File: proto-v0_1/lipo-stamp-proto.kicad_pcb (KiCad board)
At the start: 4 copper layers, 45.7 x 45.7 mm, 109 parts, among them Q1 Q_PMOS_GSD, U3 MCP73832-2-OT, U4 AP2112K-3.3, U5 AP9101CK6, U6 FS8205

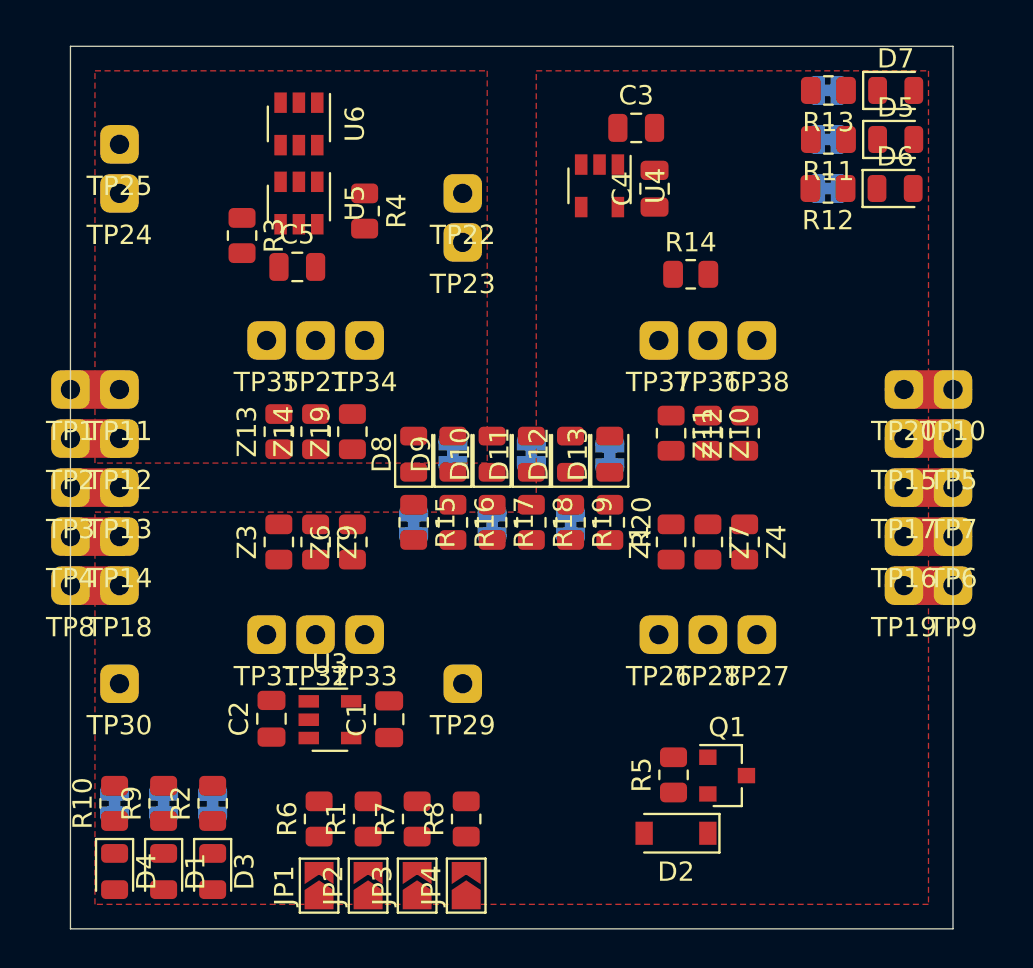
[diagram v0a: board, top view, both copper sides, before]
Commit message: Passes DRC now
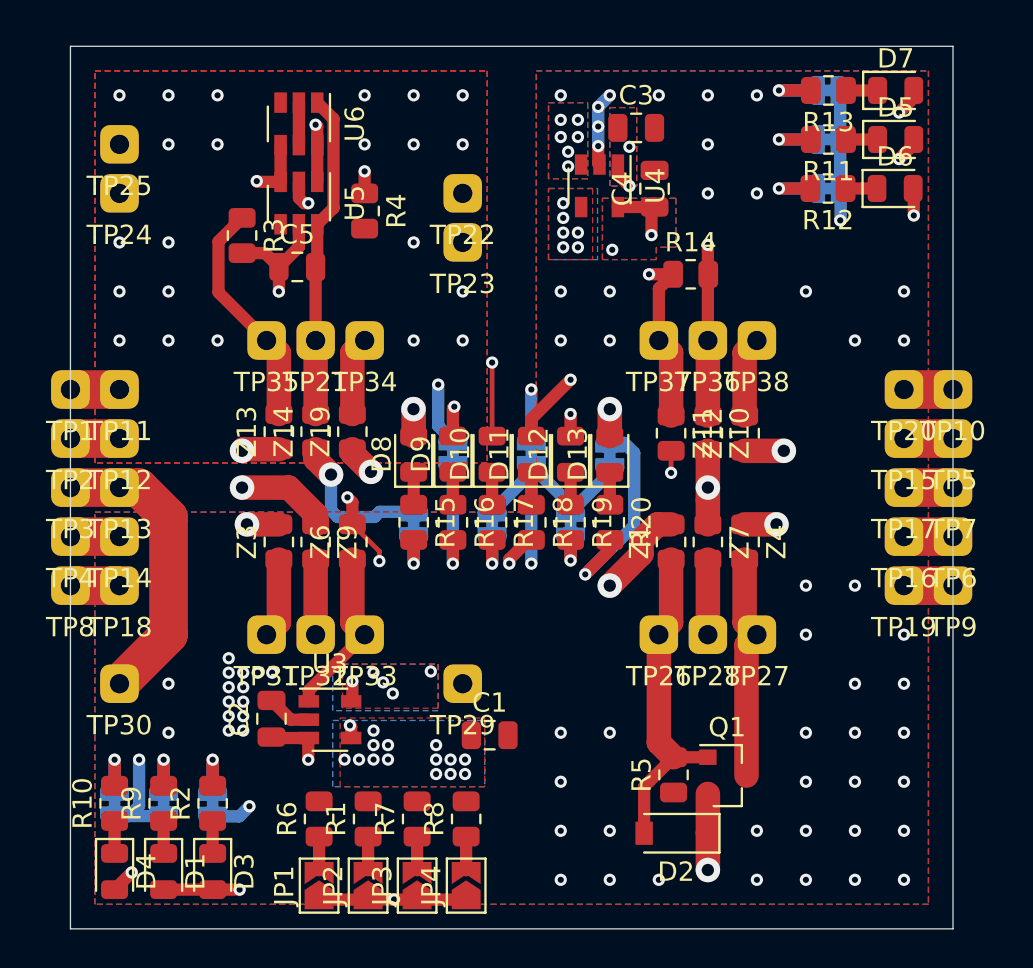
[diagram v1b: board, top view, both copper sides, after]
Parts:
- moved C1 5.27 mm to (199.5, 86.5), turned to 0 degrees
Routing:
- net GND: track 5.08 -> 69.1 mm, vias 0 -> 66
- net /+BATT: track 5.08 -> 64.8 mm, vias 0 -> 4
- net /STAT_OUT: track 2.54 -> 49.8 mm, vias 0 -> 3
- net /+CHARGE: track 2.54 -> 47.2 mm, vias 0 -> 3
- net /3V3_REG_EN: track 2.54 -> 45.5 mm, vias 0 -> 2
- net /VMAX_OUT: track 2.54 -> 41.9 mm, vias 0 -> 3
- net Net-(D7-Pad2): track 0.00 -> 36.1 mm, vias 0 -> 8
- net Net-(C3-Pad1): track 0.00 -> 29.6 mm, vias 0 -> 4
- net Net-(JP6-Pad1): track 0.00 -> 28.2 mm, vias 0 -> 1
- net Net-(C4-Pad1): track 0.00 -> 27.5 mm, vias 0 -> 3
- net Net-(JP1-Pad1): track 0.00 -> 26.8 mm, vias 0 -> 6
- net Net-(C2-Pad1): track 0.00 -> 26.4 mm, vias 0 -> 2
- net Net-(C1-Pad1): track 0.00 -> 26.4 mm, vias 0 -> 16
- net /3V3_OUT: track 2.54 -> 27.9 mm, vias 0 -> 2
- net /-BATT: track 2.54 -> 23.4 mm, vias 0 -> 1
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- added copper zone on B.Cu, net GND
- added copper zone on In1.Cu, net GND
- added copper zone on In2.Cu, net GND
- added copper zone on B.Cu, net Net-(C1-Pad1)
- added copper zone on F.Cu, net Net-(C1-Pad1)
- added copper zone on B.Cu, net Net-(C3-Pad1)
- added copper zone on F.Cu, net Net-(C3-Pad1)
- added copper zone on B.Cu, net Net-(C4-Pad1)
- added copper zone on F.Cu, net Net-(C4-Pad1)
- added copper zone on B.Cu, net Net-(D7-Pad2)
- added copper zone on F.Cu, net Net-(D7-Pad2)
- added copper zone on B.Cu, net Net-(JP1-Pad1)
- added copper zone on F.Cu, net Net-(JP1-Pad1)
- added copper zone on In1.Cu, net Net-(R4-Pad2)
- added copper zone on In2.Cu, net Net-(R4-Pad2)
- added copper zone on B.Cu, net Net-(U4-Pad4)
- added copper zone on F.Cu, net Net-(U4-Pad4)

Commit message: Almost done, just needs back silkscreen
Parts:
- JP11: value Jumper_NC_Small -> Jumper_NO_Small; footprint Jumper:SolderJumper-2_P1.3mm_Bridged_RoundedPad1.0x1.5mm -> Jumper:SolderJumper-2_P1.3mm_Open_RoundedPad1.0x1.5mm
- turned JP11 to 90 degrees
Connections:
- JP11 pad 1: /-BATT -> Net-(JP11-Pad1)
- JP11 pad 2: Net-(JP11-Pad2) -> /-BATT
- R15 pad 2: Net-(JP11-Pad2) -> Net-(JP11-Pad1)
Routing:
- net Net-(JP11-Pad2): track 2.61 -> 0.00 mm, vias 1 -> 0
- net Net-(JP11-Pad1): track 0.00 -> 2.61 mm, vias 0 -> 1
- added copper zone on B.Cu, net Net-(R4-Pad2)
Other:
- board text added: "+3v3"
- board text added: "+3v3 REG AP2112K"
- board text added: "+BAT"
- board text added: "+CH"
- board text added: "100mA 213mA"
- board text added: "3v3 EN"
- board text added: "3vEN"
- board text added: "455mA 1000mA"
- board text added: "B+"
- board text added: "B-"
- board text added: "BATT"
- board text added: "Battery Protection AP9101CK + FS8205"
- board text added: "C+"
- board text added: "CH+"
- board text added: "CH-"
- board text added: "CO"
- board text added: "Charge CTL MCP73832"
- board text added: "DO"
- board text added: "GND"
- board text added: "JLCJLCJLCJLC"
- board text added: "LiPo Stamp Proto v0.1 Nov. 2020 @bitshiftmask"
- board text added: "PROG"
- board text added: "Power Path PMOSFET + Schottky"
- board text added: "ST"
- board text added: "STAT"
- board text added: "VDD"
- board text added: "VM"
- board text added: "Vmax"

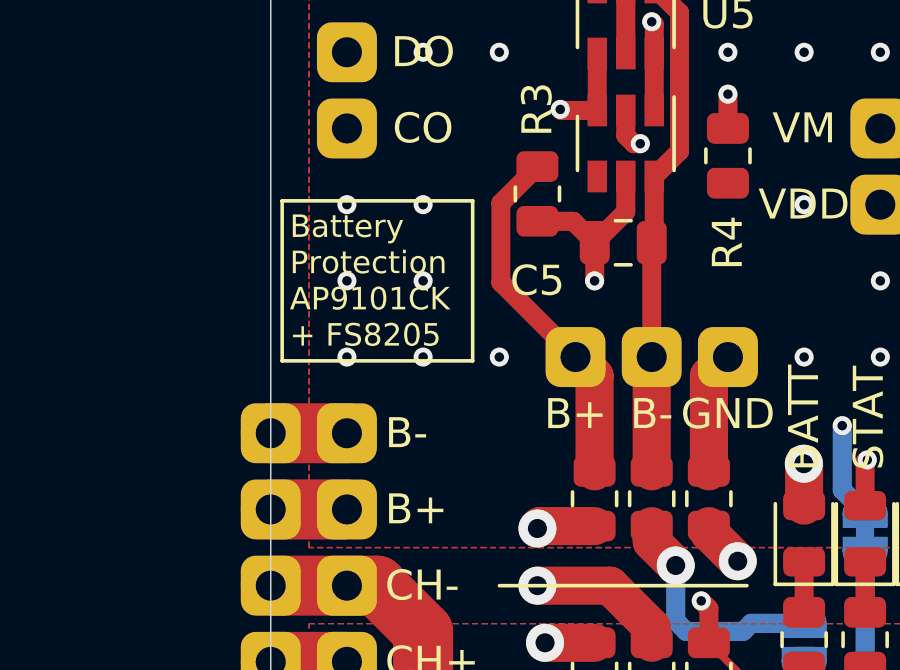
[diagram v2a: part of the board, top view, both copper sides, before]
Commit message: Add 2A polyfuse
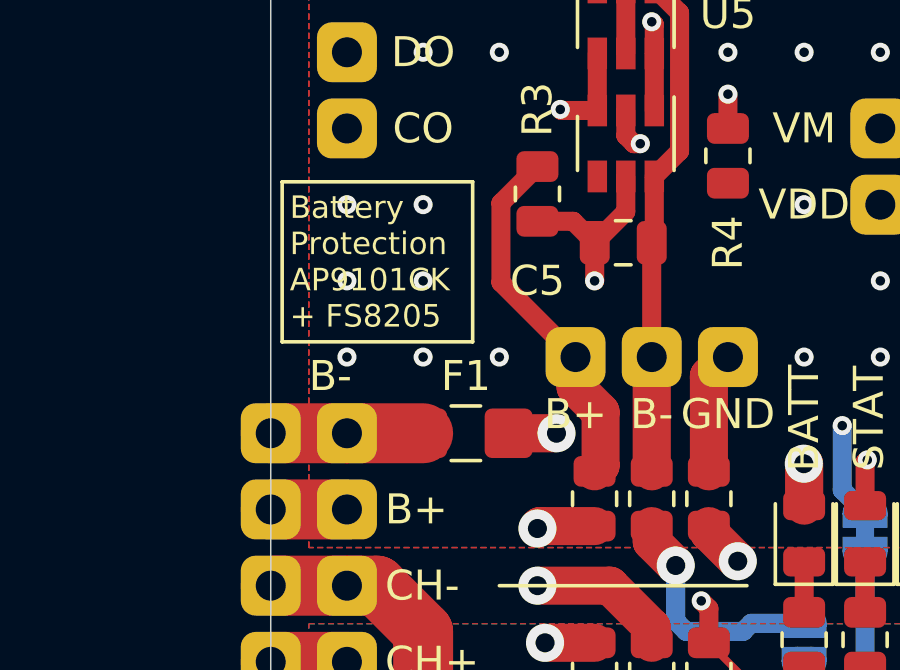
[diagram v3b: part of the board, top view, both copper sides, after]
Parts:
- added F1: Polyfuse, Fuse:Fuse_1206_3216Metric_Castellated, F.Cu at (184.3, 68.6)
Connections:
- TP1 pad 1: /-BATT -> /-BATT_RAW
- TP11 pad 1: /-BATT -> /-BATT_RAW
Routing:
- net /-BATT: track 23.4 -> 15.7 mm, vias 1 -> 2
- net /-BATT_RAW: track 0.00 -> 5.08 mm
